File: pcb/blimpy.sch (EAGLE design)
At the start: 76 parts, among them J1 MICRO-USB, J4 3-PIN SMD, J5 3-PIN SMD, J6 3-PIN SMD, J7 3-PIN SMD, Q1 mmbt2222, Q2 mmbt2222, Q3 DMG3415U, U1 RGB, U10 MAX17048, U2 AP2112-3.3, U3 MCP73831T-2, U4 BNO080, U5 SX1509, U6 SX1509, U7 CP2104, U9 ESP-WROOM-32

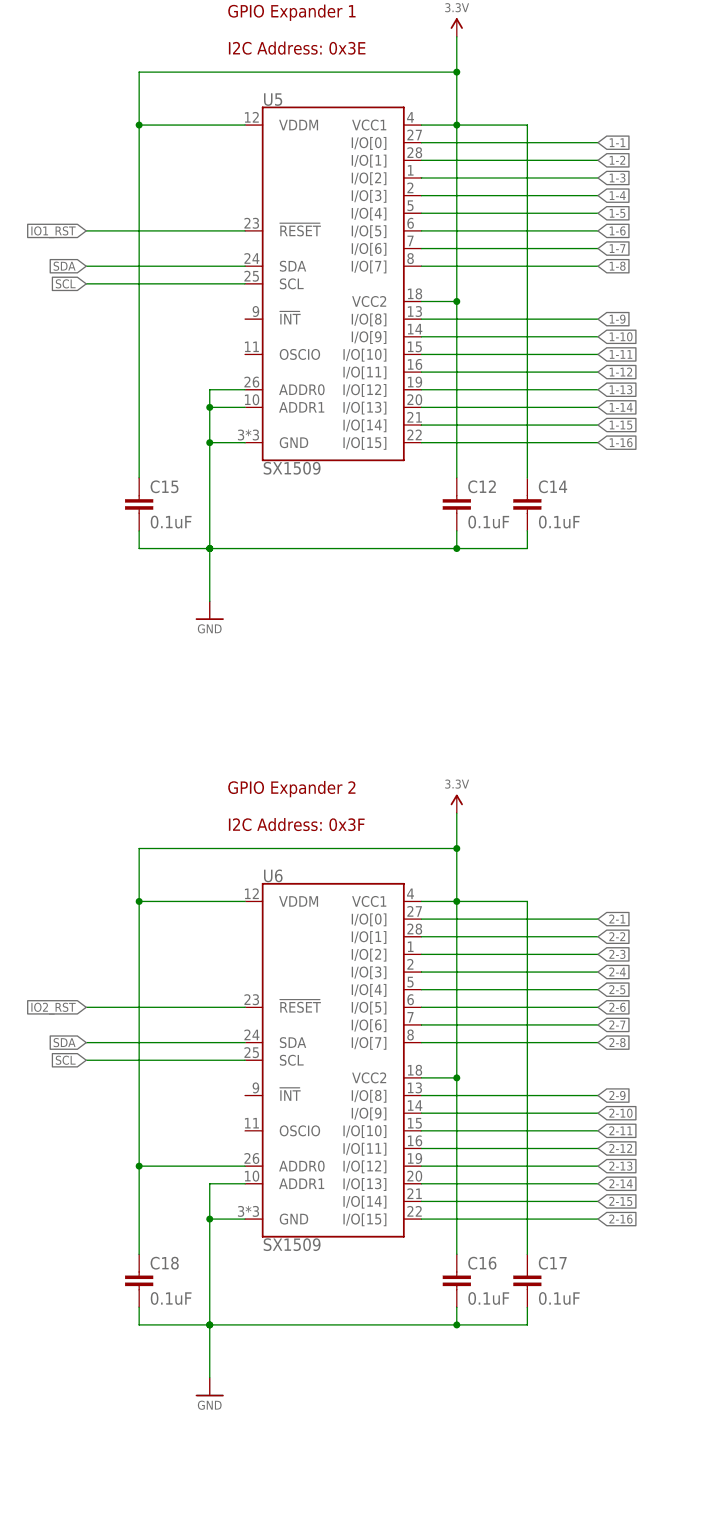
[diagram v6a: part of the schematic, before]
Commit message: fixed io capacitors
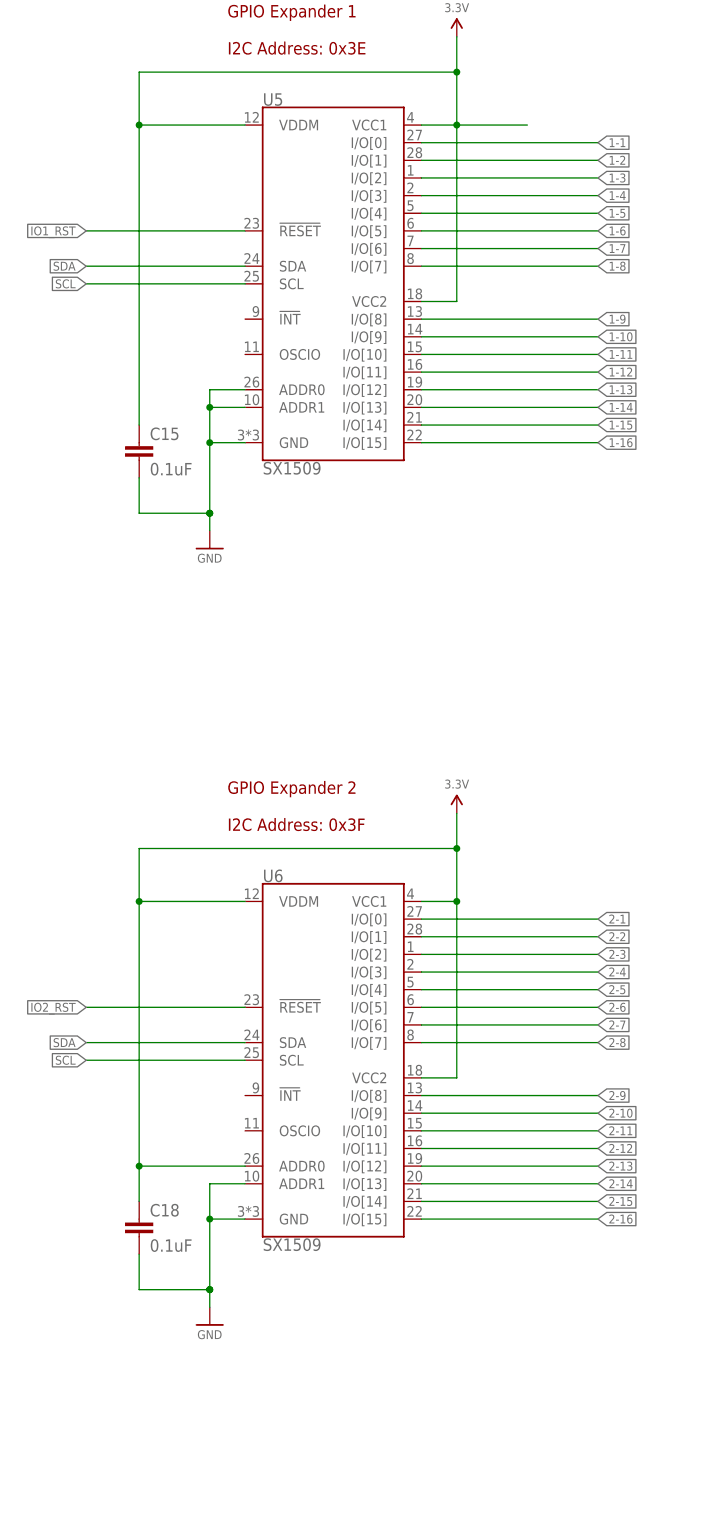
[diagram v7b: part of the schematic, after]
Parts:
- removed C12, C14, C16, C17: 0.1uF, SparkFun-Capacitors:0.1UF-0603-25V-5%
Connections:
- net 3.3V: no longer C12.1, C14.1, C16.1, C17.1
- net GND: no longer C12.2, C14.2, C16.2, C17.2
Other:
- moved on the sheet: C15, C18

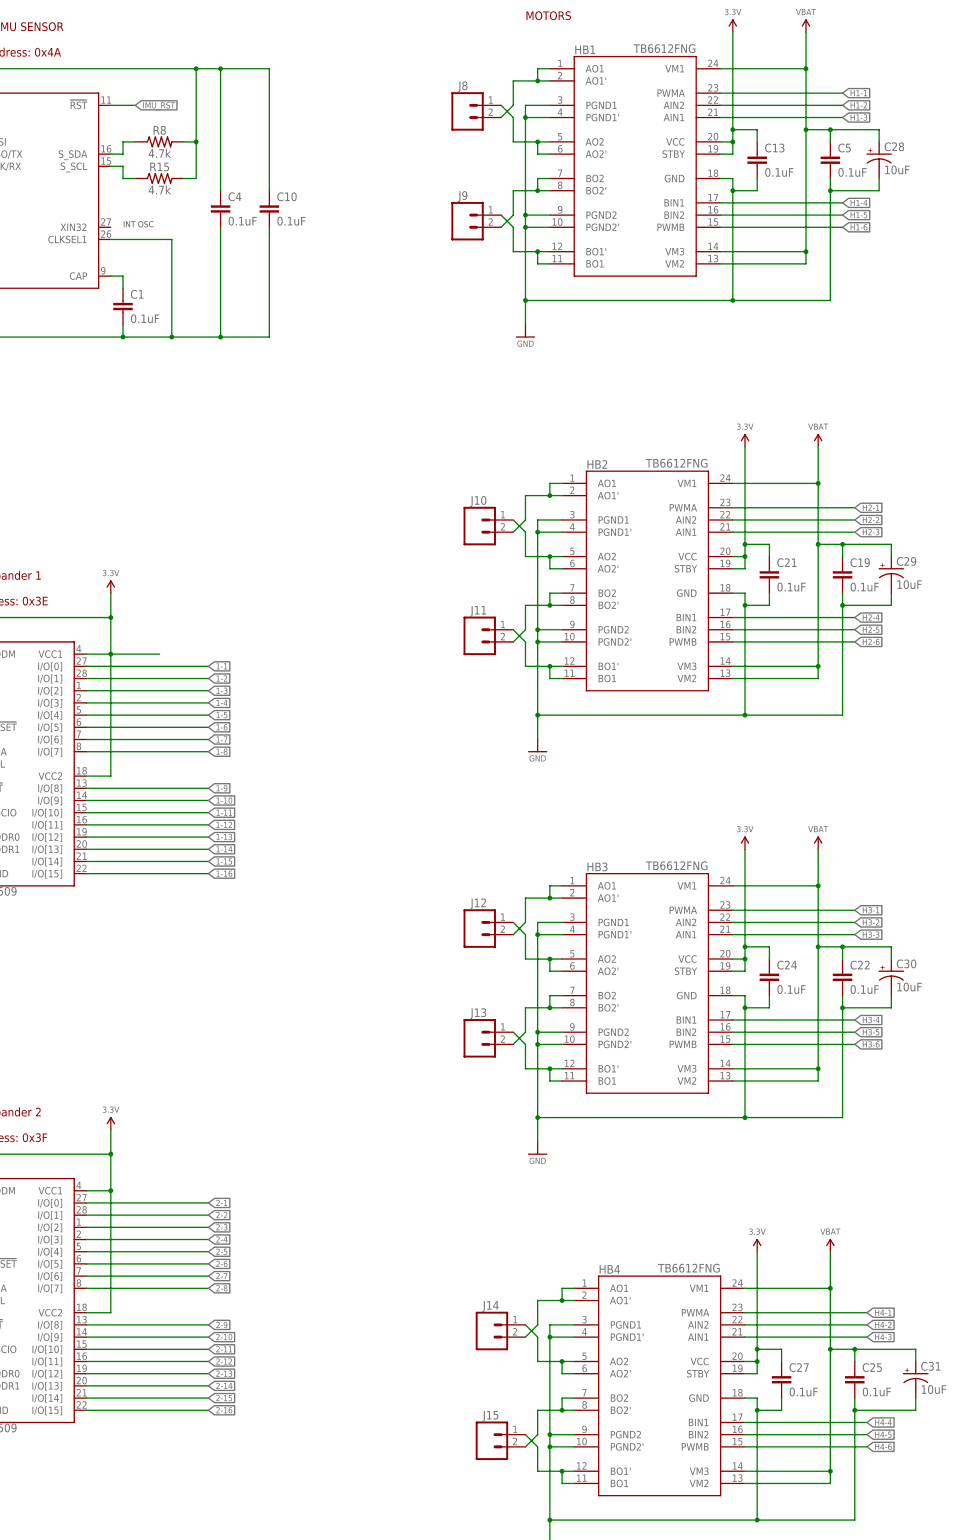
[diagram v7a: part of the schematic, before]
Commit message: finished hbridge io
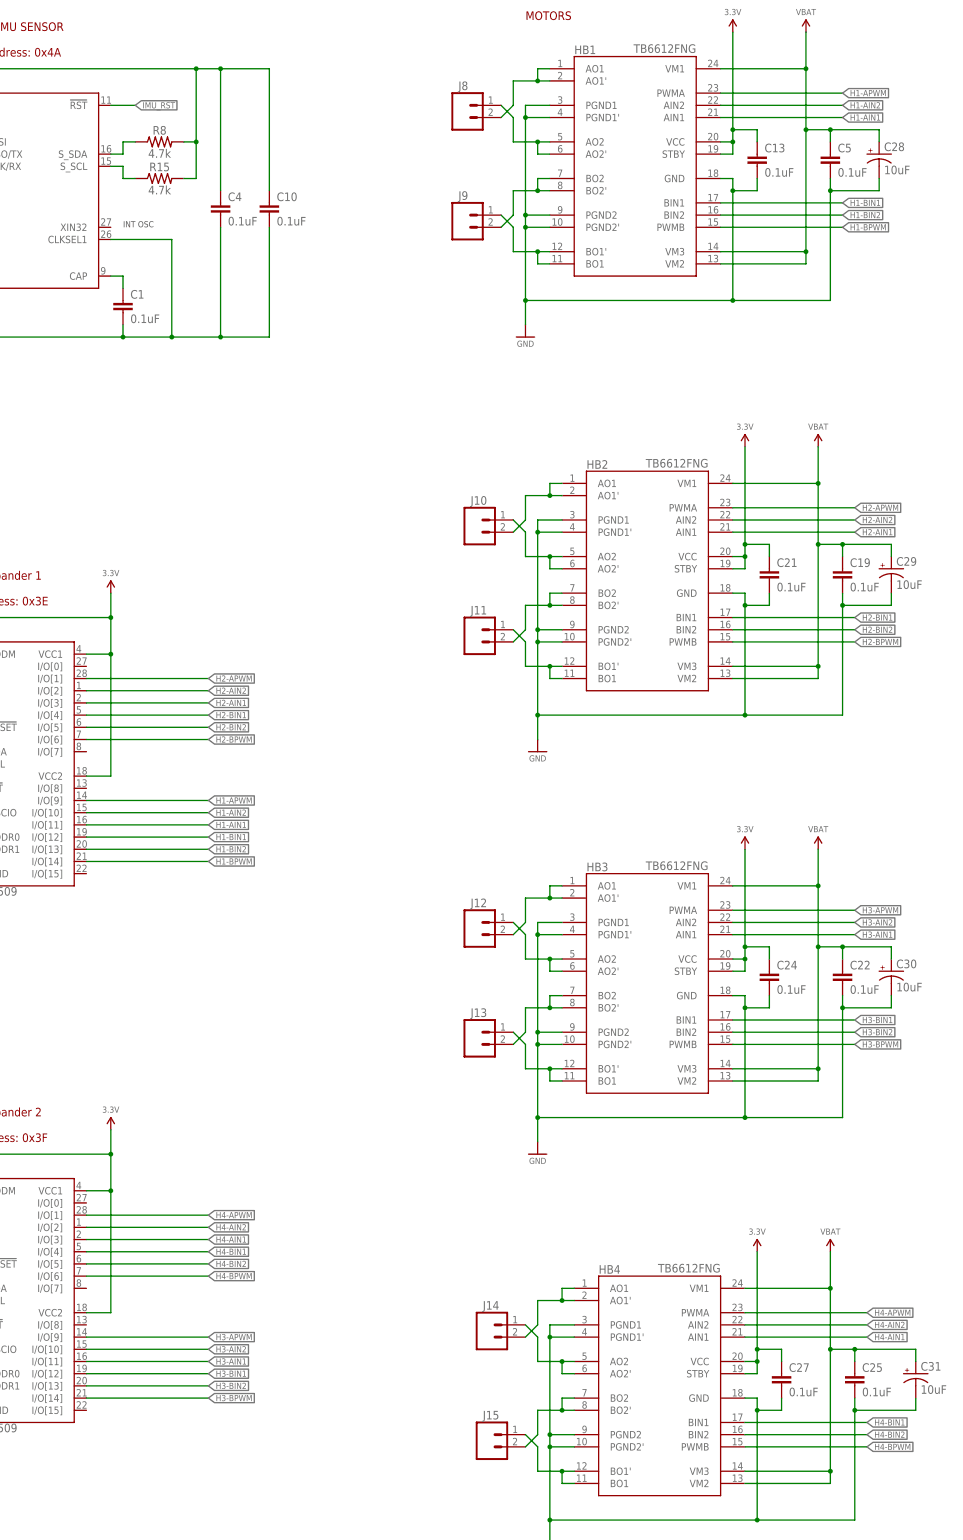
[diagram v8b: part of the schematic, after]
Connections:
- removed net 1-1: U5.I/O[0]
- removed net 1-10: U5.I/O[9]
- removed net 1-11: U5.I/O[10]
- removed net 1-12: U5.I/O[11]
- removed net 1-13: U5.I/O[12]
- removed net 1-14: U5.I/O[13]
- removed net 1-15: U5.I/O[14]
- removed net 1-16: U5.I/O[15]
- removed net 1-2: U5.I/O[1]
- removed net 1-3: U5.I/O[2]
- removed net 1-4: U5.I/O[3]
- removed net 1-5: U5.I/O[4]
- removed net 1-6: U5.I/O[5]
- removed net 1-7: U5.I/O[6]
- removed net 1-8: U5.I/O[7]
- removed net 1-9: U5.I/O[8]
- removed net 2-1: U6.I/O[0]
- removed net 2-10: U6.I/O[9]
- removed net 2-11: U6.I/O[10]
- removed net 2-12: U6.I/O[11]
- removed net 2-13: U6.I/O[12]
- removed net 2-14: U6.I/O[13]
- removed net 2-15: U6.I/O[14]
- removed net 2-16: U6.I/O[15]
- removed net 2-2: U6.I/O[1]
- removed net 2-3: U6.I/O[2]
- removed net 2-4: U6.I/O[3]
- removed net 2-5: U6.I/O[4]
- removed net 2-6: U6.I/O[5]
- removed net 2-7: U6.I/O[6]
- removed net 2-8: U6.I/O[7]
- removed net 2-9: U6.I/O[8]
- removed net H1-1: HB1.PWMA
- removed net H1-2: HB1.AIN2
- removed net H1-3: HB1.AIN1
- removed net H1-4: HB1.BIN1
- removed net H1-5: HB1.BIN2
- removed net H1-6: HB1.PWMB
- removed net H2-1: HB2.PWMA
- removed net H2-2: HB2.AIN2
- removed net H2-3: HB2.AIN1
- removed net H2-4: HB2.BIN1
- removed net H2-5: HB2.BIN2
- removed net H2-6: HB2.PWMB
- removed net H3-1: HB3.PWMA
- removed net H3-2: HB3.AIN2
- removed net H3-3: HB3.AIN1
- removed net H3-4: HB3.BIN1
- removed net H3-5: HB3.BIN2
- removed net H3-6: HB3.PWMB
- removed net H4-1: HB4.PWMA
- removed net H4-2: HB4.AIN2
- removed net H4-3: HB4.AIN1
- removed net H4-4: HB4.BIN1
- removed net H4-5: HB4.BIN2
- removed net H4-6: HB4.PWMB
- new net H1-AIN1: HB1.AIN1, U5.I/O[11]
- new net H1-AIN2: HB1.AIN2, U5.I/O[10]
- new net H1-APWM: HB1.PWMA, U5.I/O[9]
- new net H1-BIN1: HB1.BIN1, U5.I/O[12]
- new net H1-BIN2: HB1.BIN2, U5.I/O[13]
- new net H1-BPWM: HB1.PWMB, U5.I/O[14]
- new net H2-AIN1: HB2.AIN1, U5.I/O[3]
- new net H2-AIN2: HB2.AIN2, U5.I/O[2]
- new net H2-APWM: HB2.PWMA, U5.I/O[1]
- new net H2-BIN1: HB2.BIN1, U5.I/O[4]
- new net H2-BIN2: HB2.BIN2, U5.I/O[5]
- new net H2-BPWM: HB2.PWMB, U5.I/O[6]
- new net H3-AIN1: HB3.AIN1, U6.I/O[11]
- new net H3-AIN2: HB3.AIN2, U6.I/O[10]
- new net H3-APWM: HB3.PWMA, U6.I/O[9]
- new net H3-BIN1: HB3.BIN1, U6.I/O[12]
- new net H3-BIN2: HB3.BIN2, U6.I/O[13]
- new net H3-BPWM: HB3.PWMB, U6.I/O[14]
- new net H4-AIN1: HB4.AIN1, U6.I/O[3]
- new net H4-AIN2: HB4.AIN2, U6.I/O[2]
- new net H4-APWM: HB4.PWMA, U6.I/O[1]
- new net H4-BIN1: HB4.BIN1, U6.I/O[4]
- new net H4-BIN2: HB4.BIN2, U6.I/O[5]
- new net H4-BPWM: HB4.PWMB, U6.I/O[6]
